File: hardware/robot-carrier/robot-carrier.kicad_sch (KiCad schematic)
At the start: 34 parts, among them J1 6S BATTERY INPUT, J10 M1 JGA25-2430-CE, J100 PROTECTED 6S BATTERY, J101 EXTERNAL BUCK 5V OUTPUT, J11 M2 JGA25-2430-CE, J12 M3 JGA25-2430-CE, J13 M4 JGA25-2430-CE, J2 BUCK INPUT 24V, J20 SERVO 1, J21 SERVO 2, J22 SERVO 3, J23 SERVO 4, J3 BUCK OUTPUT 5V, J30 WT901 UART, J40 GA25 L298N LOGIC, J41 GA25 L298N POWER

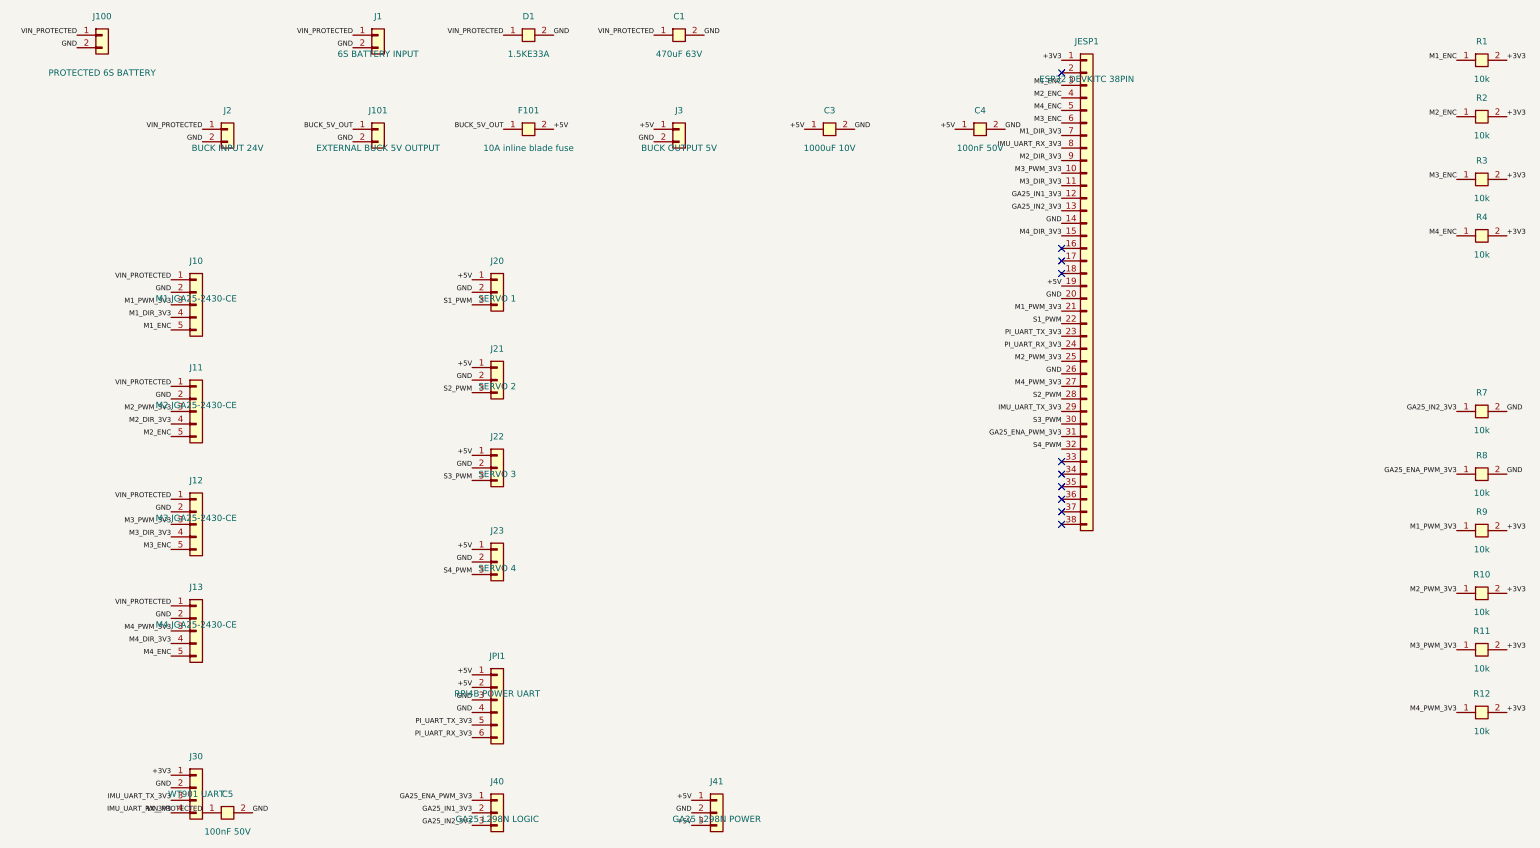
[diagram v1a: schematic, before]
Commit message: Adapt carrier for 30-pin ESP32 DevKit
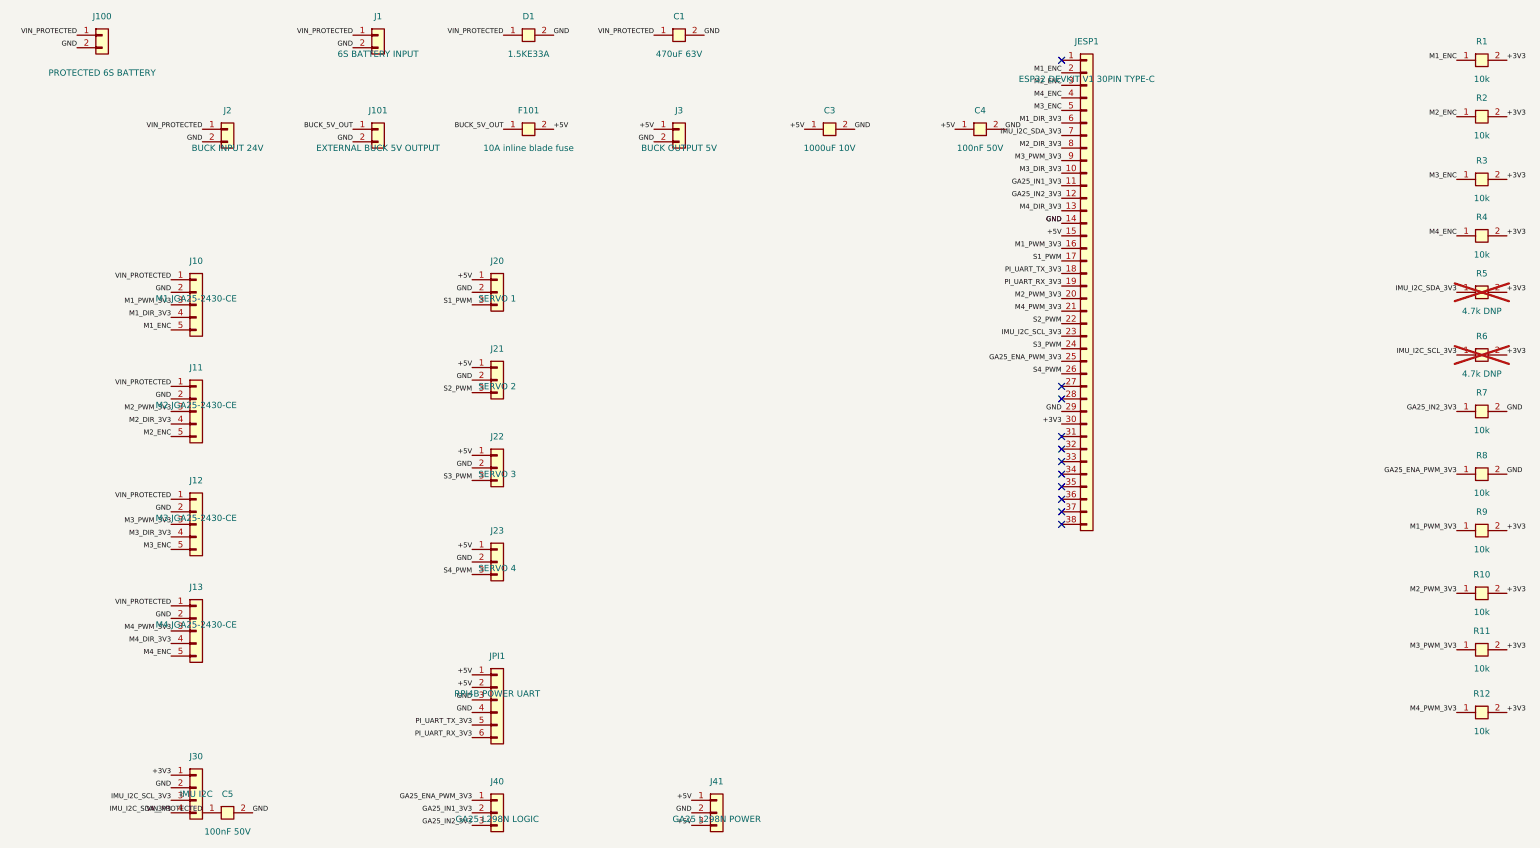
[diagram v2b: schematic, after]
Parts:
- added R5, R6: 4.7k DNP, Custom:R_1206_HAND, symbol RobotCarrier:R
- J30: value WT901 UART -> IMU I2C
- JESP1: value ESP32 DEVKITC 38PIN -> ESP32 DEVKIT V1 30PIN TYPE-C; footprint Custom:ESP32_DEVKITC_38PIN_SOCKET -> Custom:ESP32_DEVKIT_V1_30PIN_SOCKET
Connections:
- net +3V3: now also JESP1.30 (Pin_30), R5.2 (Pin_2), R6.2 (Pin_2); no longer JESP1.1 (Pin_1)
- net +5V: now also JESP1.15 (Pin_15); no longer JESP1.19 (Pin_19)
- net GA25_ENA_PWM_3V3: now also JESP1.25 (Pin_25); no longer JESP1.31 (Pin_31)
- net GA25_IN1_3V3: now also JESP1.11 (Pin_11); no longer JESP1.12 (Pin_12)
- net GA25_IN2_3V3: now also JESP1.12 (Pin_12); no longer JESP1.13 (Pin_13)
- net GND: now also JESP1.29 (Pin_29); no longer JESP1.20 (Pin_20), JESP1.26 (Pin_26)
- net M1_DIR_3V3: now also JESP1.6 (Pin_6); no longer JESP1.7 (Pin_7)
- net M1_ENC: now also JESP1.2 (Pin_2); no longer JESP1.3 (Pin_3)
- net M1_PWM_3V3: now also JESP1.16 (Pin_16); no longer JESP1.21 (Pin_21)
- net M2_DIR_3V3: now also JESP1.8 (Pin_8); no longer JESP1.9 (Pin_9)
- net M2_ENC: now also JESP1.3 (Pin_3); no longer JESP1.4 (Pin_4)
- net M2_PWM_3V3: now also JESP1.20 (Pin_20); no longer JESP1.25 (Pin_25)
- net M3_DIR_3V3: now also JESP1.10 (Pin_10); no longer JESP1.11 (Pin_11)
- net M3_ENC: now also JESP1.5 (Pin_5); no longer JESP1.6 (Pin_6)
- net M3_PWM_3V3: now also JESP1.9 (Pin_9); no longer JESP1.10 (Pin_10)
- net M4_DIR_3V3: now also JESP1.13 (Pin_13); no longer JESP1.15 (Pin_15)
- net M4_ENC: now also JESP1.4 (Pin_4); no longer JESP1.5 (Pin_5)
- net M4_PWM_3V3: now also JESP1.21 (Pin_21); no longer JESP1.27 (Pin_27)
- net PI_UART_RX_3V3: now also JESP1.19 (Pin_19); no longer JESP1.24 (Pin_24)
- net PI_UART_TX_3V3: now also JESP1.18 (Pin_18); no longer JESP1.23 (Pin_23)
- net S1_PWM: now also JESP1.17 (Pin_17); no longer JESP1.22 (Pin_22)
- net S2_PWM: now also JESP1.22 (Pin_22); no longer JESP1.28 (Pin_28)
- net S3_PWM: now also JESP1.24 (Pin_24); no longer JESP1.30 (Pin_30)
- net S4_PWM: now also JESP1.26 (Pin_26); no longer JESP1.32 (Pin_32)
- net IMU_UART_RX_3V3 renamed IMU_I2C_SDA_3V3
- net IMU_I2C_SDA_3V3: now also JESP1.7 (Pin_7), R5.1 (Pin_1); no longer JESP1.8 (Pin_8)
- net IMU_UART_TX_3V3 renamed IMU_I2C_SCL_3V3
- net IMU_I2C_SCL_3V3: now also JESP1.23 (Pin_23), R6.1 (Pin_1); no longer JESP1.29 (Pin_29)
- no-connect marks 10 -> 11
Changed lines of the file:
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@@
 			)
 		)
-		(property "Value" "WT901 UART"
+		(property "Value" "IMU I2C"
 			(at 39.37 179.07 0)
 				(effects
@@
 			)
 		)
-		(property "Description" "WT901 UART"
+		(property "Description" "IMU I2C"
 			(at 39.37 175.26 0)
 				(effects
@@
 		)
 	)
-	(label "IMU_UART_TX_3V3"
+	(label "IMU_I2C_SCL_3V3"
 		(at 34.29 180.34 180)
 			(effects
@@
 		)
 	)
-	(label "IMU_UART_RX_3V3"
+	(label "IMU_I2C_SDA_3V3"
 		(at 34.29 182.88 180)
 			(effects
@@
 			)
 		)
-		(property "Value" "ESP32 DEVKITC 38PIN"
+		(property "Value" "ESP32 DEVKIT V1 30PIN TYPE-C"
 			(at 219.71 34.29 0)
 				(effects
@@
 			)
 		)
-		(property "Footprint" "Custom:ESP32_DEVKITC_38PIN_SOCKET"
+		(property "Footprint" "Custom:ESP32_DEVKIT_V1_30PIN_SOCKET"
 			(at 219.71 30.48 0)
 				(effects
@@
 			)
 		)
-		(property "Description" "ESP32 DEVKITC 38PIN"
+		(property "Description" "ESP32-WROOM-32 DevKit V1 30-pin Type-C; generic connector pins 31-38 unused"
 			(at 219.71 30.48 0)
 				(effects
@@
 	)
 	(label "+3V3"
-		(at 214.63 30.48 180)
+		(at 214.63 104.14 180)
 			(effects
 			(font
@@
 	)
 	(label "M1_ENC"
+		(at 214.63 33.02 180)
+			(effects
+			(font
+				(size 1 1)
+			)
+			(justify right bottom)
+		)
+	)
+	(label "M2_ENC"
 		(at 214.63 35.56 180)
 			(effects
@@
 		)
 	)
-	(label "M2_ENC"
+	(label "M4_ENC"
 		(at 214.63 38.1 180)
 			(effects
@@
 		)
 	)
-	(label "M4_ENC"
+	(label "M3_ENC"
 		(at 214.63 40.64 180)
 			(effects
@@
 		)
 	)
-	(label "M3_ENC"
+	(label "M1_DIR_3V3"
 		(at 214.63 43.18 180)
 			(effects
@@
 		)
 	)
-	(label "M1_DIR_3V3"
+	(label "IMU_I2C_SDA_3V3"
 		(at 214.63 45.72 180)
 			(effects
@@
 		)
 	)
-	(label "IMU_UART_RX_3V3"
+	(label "M2_DIR_3V3"
 		(at 214.63 48.26 180)
 			(effects
@@
 		)
 	)
-	(label "M2_DIR_3V3"
+	(label "M3_PWM_3V3"
 		(at 214.63 50.8 180)
 			(effects
@@
 		)
 	)
-	(label "M3_PWM_3V3"
+	(label "M3_DIR_3V3"
 		(at 214.63 53.34 180)
 			(effects
@@
 		)
 	)
-	(label "M3_DIR_3V3"
+	(label "GA25_IN1_3V3"
 		(at 214.63 55.88 180)
 			(effects
@@
 		)
 	)
-	(label "GA25_IN1_3V3"
+	(label "GA25_IN2_3V3"
 		(at 214.63 58.42 180)
-			(effects
-			(font
-				(size 1 1)
-			)
-			(justify right bottom)
-		)
-	)
-	(label "GA25_IN2_3V3"
-		(at 214.63 60.96 180)
 			(effects
 			(font
@@
 	)
 	(label "M4_DIR_3V3"
+		(at 214.63 60.96 180)
+			(effects
+			(font
+				(size 1 1)
+			)
+			(justify right bottom)
+		)
+	)
+	(label "+5V"
 		(at 214.63 66.04 180)
 			(effects
@@
 		)
 	)
-	(label "+5V"
+	(label "GND"
+		(at 214.63 101.6 180)
+			(effects
+			(font
+				(size 1 1)
+			)
+			(justify right bottom)
+		)
+	)
+	(label "M1_PWM_3V3"
+		(at 214.63 68.58 180)
+			(effects
+			(font
+				(size 1 1)
+			)
+			(justify right bottom)
+		)
+	)
+	(label "S1_PWM"
+		(at 214.63 71.12 180)
+			(effects
+			(font
+				(size 1 1)
+			)
+			(justify right bottom)
+		)
+	)
+	(label "PI_UART_TX_3V3"
+		(at 214.63 73.66 180)
+			(effects
+			(font
+				(size 1 1)
+			)
+			(justify right bottom)
+		)
+	)
+	(label "PI_UART_RX_3V3"
 		(at 214.63 76.2 180)
 			(effects
@@
 		)
 	)
+	(label "M2_PWM_3V3"
+		(at 214.63 78.74 180)
+			(effects
+			(font
+				(size 1 1)
+			)
+			(justify right bottom)
+		)
+	)
 	(label "GND"
-		(at 214.63 78.74 180)
-			(effects
-			(font
-				(size 1 1)
-			)
-			(justify right bottom)
-		)
-	)
-	(label "M1_PWM_3V3"
+		(at 214.63 63.5 180)
+			(effects
+			(font
+				(size 1 1)
+			)
+			(justify right bottom)
+		)
+	)
+	(label "M4_PWM_3V3"
 		(at 214.63 81.28 180)
 			(effects
@@
 		)
 	)
-	(label "S1_PWM"
+	(label "S2_PWM"
 		(at 214.63 83.82 180)
 			(effects
@@
 		)
 	)
-	(label "PI_UART_TX_3V3"
+	(label "IMU_I2C_SCL_3V3"
 		(at 214.63 86.36 180)
 			(effects
@@
 		)
 	)
-	(label "PI_UART_RX_3V3"
+	(label "S3_PWM"
 		(at 214.63 88.9 180)
 			(effects
@@
 		)
 	)
-	(label "M2_PWM_3V3"
+	(label "GA25_ENA_PWM_3V3"
 		(at 214.63 91.44 180)
 			(effects
@@
 		)
 	)
-	(label "GND"
+	(label "S4_PWM"
 		(at 214.63 93.98 180)
-			(effects
-			(font
-				(size 1 1)
-			)
-			(justify right bottom)
-		)
-	)
-	(label "M4_PWM_3V3"
-		(at 214.63 96.52 180)
-			(effects
-			(font
-				(size 1 1)
-			)
-			(justify right bottom)
-		)
-	)
-	(label "S2_PWM"
-		(at 214.63 99.06 180)
-			(effects
-			(font
-				(size 1 1)
-			)
-			(justify right bottom)
-		)
-	)
-	(label "IMU_UART_TX_3V3"
-		(at 214.63 101.6 180)
-			(effects
-			(font
-				(size 1 1)
-			)
-			(justify right bottom)
-		)
-	)
-	(label "S3_PWM"
-		(at 214.63 104.14 180)
-			(effects
-			(font
-				(size 1 1)
-			)
-			(justify right bottom)
-		)
-	)
-	(label "GA25_ENA_PWM_3V3"
-		(at 214.63 106.68 180)
-			(effects
-			(font
-				(size 1 1)
-			)
-			(justify right bottom)
-		)
-	)
-	(label "S4_PWM"
-		(at 214.63 109.22 180)
 			(effects
 			(font
@@
 	(symbol
 		(lib_id "RobotCarrier:R")
+		(at 299.72 77.47 0)
+		(unit 1)
+		(exclude_from_sim no)
+		(in_bom yes)
+		(on_board yes)
+		(dnp yes)
+		(property "Reference" "R5"
+			(at 299.72 73.66 0)
+				(effects (font (size 1.27 1.27)))
+		)
+		(property "Value" "4.7k DNP"
+			(at 299.72 81.28 0)
+				(effects (font (size 1.27 1.27)))
+		)
+		(property "Footprint" "Custom:R_1206_HAND"
+			(at 299.72 77.47 0)
+				(effects (font (size 1.27 1.27)) (hide yes))
+		)
+		(property "Datasheet" "~"
+			(at 299.72 77.47 0)
+				(effects (font (size 1.27 1.27)) (hide yes))
+		)
+		(property "Description" "Optional I2C SDA pull-up"
+			(at 299.72 77.47 0)
+				(effects (font (size 1.27 1.27)) (hide yes))
+		)
+		(property "LCSC" "C17936"
+			(at 299.72 77.47 0)
+				(effects (font (size 1.27 1.27)) (hide yes))
+		)
+		(pin "1")
+		(pin "2")
+		(instances
+			(project "robot-carrier"
+				(path "/00000000-0000-4000-8000-000000000001"
+					(reference "R5")
+					(unit 1)
+				)
+			)
+		)
+	)
+	(label "IMU_I2C_SDA_3V3"
+		(at 294.64 77.47 180)
+			(effects (font (size 1 1)) (justify right bottom))
+	)
+	(label "+3V3"
+		(at 304.8 77.47 0)
+			(effects (font (size 1 1)) (justify left bottom))
+	)
+	(symbol
+		(lib_id "RobotCarrier:R")
+		(at 299.72 90.17 0)
+		(unit 1)
+		(exclude_from_sim no)
+		(in_bom yes)
+		(on_board yes)
+		(dnp yes)
+		(property "Reference" "R6"
+			(at 299.72 86.36 0)
+				(effects (font (size 1.27 1.27)))
+		)
+		(property "Value" "4.7k DNP"
+			(at 299.72 93.98 0)
+				(effects (font (size 1.27 1.27)))
+		)
+		(property "Footprint" "Custom:R_1206_HAND"
+			(at 299.72 90.17 0)
+				(effects (font (size 1.27 1.27)) (hide yes))
+		)
+		(property "Datasheet" "~"
+			(at 299.72 90.17 0)
+				(effects (font (size 1.27 1.27)) (hide yes))
+		)
+		(property "Description" "Optional I2C SCL pull-up"
+			(at 299.72 90.17 0)
+				(effects (font (size 1.27 1.27)) (hide yes))
+		)
+		(property "LCSC" "C17936"
+			(at 299.72 90.17 0)
+				(effects (font (size 1.27 1.27)) (hide yes))
+		)
+		(pin "1")
+		(pin "2")
+		(instances
+			(project "robot-carrier"
+				(path "/00000000-0000-4000-8000-000000000001"
+					(reference "R6")
+					(unit 1)
+				)
+			)
+		)
+	)
+	(label "IMU_I2C_SCL_3V3"
+		(at 294.64 90.17 180)
+			(effects (font (size 1 1)) (justify right bottom))
+	)
+	(label "+3V3"
+		(at 304.8 90.17 0)
+			(effects (font (size 1 1)) (justify left bottom))
+	)
+	(symbol
+		(lib_id "RobotCarrier:R")
 		(at 299.72 101.6 0)
 		(unit 1)
@@
 	)
 	(no_connect
-		(at 214.63 33.02)
+		(at 214.63 30.48)
 	)
 	(no_connect
-		(at 214.63 68.58)
+		(at 214.63 96.52)
 	)
 	(no_connect
-		(at 214.63 71.12)
+		(at 214.63 99.06)
 	)
 	(no_connect
-		(at 214.63 73.66)
+		(at 214.63 106.68)
 	)
 	(no_connect
@@
 	)
 	(no_connect
+		(at 214.63 109.22)
+	)
+	(no_connect

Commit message: updated
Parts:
- C3: value 1000uF 10V -> 1000uF 16V; LCSC C79119 -> C51934166
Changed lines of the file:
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@@
 			)
 		)
-		(property "Value" "1000uF 10V"
+		(property "Value" "1000uF 16V"
 			(at 167.64 48.26 0)
 				(effects
@@
 			)
 		)
-		(property "Description" "1000uF 10V"
+		(property "Description" "1000uF 16V low-ESR polymer, JIERR PB16V1000M8X15"
 			(at 167.64 44.45 0)
 				(effects
@@
 			)
 		)
-		(property "LCSC" "C79119"
+		(property "LCSC" "C51934166"
 			(at 167.64 44.45 0)
 				(effects

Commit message: Use 2200uF
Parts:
- R1, R10, R11, R12, R2, R3, R4, R5, R6, R7, R8, R9: footprint Custom:R_1206_HAND -> Custom:R_0805_HAND
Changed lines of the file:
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@@
 			)
 		)
-		(property "Footprint" "Custom:R_1206_HAND"
+		(property "Footprint" "Custom:R_0805_HAND"
 			(at 299.72 30.48 0)
 				(effects
@@
 			)
 		)
-		(property "Footprint" "Custom:R_1206_HAND"
+		(property "Footprint" "Custom:R_0805_HAND"
 			(at 299.72 41.91 0)
 				(effects
@@
 			)
 		)
-		(property "Footprint" "Custom:R_1206_HAND"
+		(property "Footprint" "Custom:R_0805_HAND"
 			(at 299.72 54.61 0)
 				(effects
@@
 			)
 		)
-		(property "Footprint" "Custom:R_1206_HAND"
+		(property "Footprint" "Custom:R_0805_HAND"
 			(at 299.72 66.04 0)
 				(effects
@@
 				(effects (font (size 1.27 1.27)))
 		)
-		(property "Footprint" "Custom:R_1206_HAND"
+		(property "Footprint" "Custom:R_0805_HAND"
 			(at 299.72 77.47 0)
 				(effects (font (size 1.27 1.27)) (hide yes))
@@
 				(effects (font (size 1.27 1.27)))
 		)
-		(property "Footprint" "Custom:R_1206_HAND"
+		(property "Footprint" "Custom:R_0805_HAND"
 			(at 299.72 90.17 0)
 				(effects (font (size 1.27 1.27)) (hide yes))
@@
 			)
 		)
-		(property "Footprint" "Custom:R_1206_HAND"
+		(property "Footprint" "Custom:R_0805_HAND"
 			(at 299.72 101.6 0)
 				(effects
@@
 			)
 		)
-		(property "Footprint" "Custom:R_1206_HAND"
+		(property "Footprint" "Custom:R_0805_HAND"
 			(at 299.72 114.3 0)
 				(effects
@@
 			)
 		)
-		(property "Footprint" "Custom:R_1206_HAND"
+		(property "Footprint" "Custom:R_0805_HAND"
 			(at 299.72 125.73 0)
 				(effects
@@
 			)
 		)
-		(property "Footprint" "Custom:R_1206_HAND"
+		(property "Footprint" "Custom:R_0805_HAND"
 			(at 299.72 138.43 0)
 				(effects
@@
 			)
 		)
-		(property "Footprint" "Custom:R_1206_HAND"
+		(property "Footprint" "Custom:R_0805_HAND"
 			(at 299.72 149.86 0)
 				(effects
@@
 			)
 		)
-		(property "Footprint" "Custom:R_1206_HAND"
+		(property "Footprint" "Custom:R_0805_HAND"
 			(at 299.72 162.56 0)
 				(effects
